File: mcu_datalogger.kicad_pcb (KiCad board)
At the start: 2 copper layers, 29 parts, among them J1 Conn_01x04_Pin, J2 Conn_01x04_Pin, J3 Conn_01x09_Pin, J4 Conn_02x03_Odd_Even, U1 24LC1025, U2 DS1337S_, U3 24LC1025, U4 ATMEGA328P-AU_SL044, Y1 32.768 KHz, Y2 16 MHz

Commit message: PCB v1
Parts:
- moved U3 38.7 mm to (161.1, 68.1), turned to -90 degrees
- moved R7 37.5 mm to (168.2, 87.0), turned to 180 degrees
- moved U1 37.5 mm to (167.1, 68.1), turned to -90 degrees
- moved R5 36.2 mm to (168.2, 89.0), turned to 180 degrees
- moved R3 34.6 mm to (165.3, 75.6), turned to 90 degrees
- moved R4 33.3 mm to (162.9, 75.6), turned to 90 degrees
- moved R6 30.4 mm to (155.4, 74.7), turned to -90 degrees
- moved Y2 28.5 mm to (146.9, 83.4), turned to 90 degrees
- moved J4 27.6 mm to (150.8, 67.8), turned to 90 degrees
- moved R1 27.1 mm to (154.6, 94.6), turned to 90 degrees
- moved C4 26.4 mm to (168.2, 85.0), turned to 180 degrees
- moved R2 25.9 mm to (152.5, 98.4), turned to 90 degrees
- moved J2 25.7 mm to (146.8, 65.3)
- moved C5 24.4 mm to (164.7, 87.0)
- moved Y1 23.1 mm to (156.7, 90.7)
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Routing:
- net GND: track 0.00 -> 194.3 mm, vias 0 -> 6
- net /Vcc: track 0.00 -> 139.6 mm, vias 0 -> 2
- net /SCK: track 0.00 -> 84.2 mm, vias 0 -> 2
- net /SDA: track 0.00 -> 66.4 mm, vias 0 -> 2
- net /D8: track 0.00 -> 30.9 mm, vias 0 -> 2
- net /D5: track 0.00 -> 30.6 mm, vias 0 -> 2
- net /D7: track 0.00 -> 30.4 mm, vias 0 -> 2
- net /D6: track 0.00 -> 30.1 mm, vias 0 -> 2
- net /MOSI: track 0.00 -> 26.0 mm, vias 0 -> 2
- net /MISO: track 0.00 -> 25.7 mm, vias 0 -> 2
- net /D4: track 0.00 -> 22.4 mm, vias 0 -> 2
- net /D2: track 0.00 -> 22.3 mm, vias 0 -> 2
- net /D3: track 0.00 -> 22.0 mm, vias 0 -> 2
- net Net-(BT1-+): track 0.00 -> 19.3 mm
- net /RX: track 0.00 -> 13.0 mm
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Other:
- board outline added: 30.3 x 39.1 mm

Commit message: PCB v2
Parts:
- moved H1 65.9 mm to (175.2, 60.8)
- moved H4 51.1 mm to (175.2, 102.0)
- moved H3 28.2 mm to (142.8, 102.0)
- moved H2 27.9 mm to (142.8, 60.8)
- moved BT1 17.0 mm to (164.6, 99.0)
- moved C1 0.68 mm to (154.3, 97.7)
- moved C2 0.68 mm to (146.6, 77.1)
- moved C4 0.68 mm to (167.9, 84.4)
- moved C5 0.68 mm to (164.4, 86.4)
- moved D1 0.68 mm to (164.4, 88.4)
- moved D2 0.68 mm to (164.4, 84.4)
- moved J1 0.68 mm to (171.9, 64.7)
- moved J3 0.68 mm to (171.9, 75.9)
- moved R1 0.68 mm to (154.3, 93.9)
- moved R2 0.68 mm to (152.2, 97.7)
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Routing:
- net Net-(BT1-+): track 19.3 -> 59.8 mm, vias 0 -> 2
- net Net-(U4-AREF): track 11.6 -> 8.68 mm, vias 0 -> 2
- net /D4: track 22.4 -> 21.1 mm

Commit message: PCB final
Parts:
- moved J3 25.4 mm to (146.5, 76.0)
- moved Y2 20.1 mm to (166.7, 82.9)
- moved C2 17.3 mm to (163.7, 80.0), turned to -90 degrees
- moved C3 17.3 mm to (163.7, 85.8), turned to 90 degrees
- moved C4 10.5 mm to (167.3, 94.9), turned to 0 degrees
- moved D2 7.14 mm to (167.3, 90.9)
- moved D1 6.56 mm to (163.8, 94.9)
- moved R7 6.55 mm to (167.3, 92.9), turned to 0 degrees
- moved R5 6.10 mm to (163.8, 92.9)
- moved C5 4.57 mm to (163.8, 90.9)
- moved J1 1.13 mm to (171.8, 65.8)
- moved R1 1.12 mm to (153.3, 93.5), turned to 0 degrees
- moved H1 0.28 mm to (175.0, 61.0)
- moved H2 0.28 mm to (143.0, 61.0)
- moved H3 0.20 mm to (143.0, 102.0)
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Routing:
- net GND: track 194.2 -> 166.9 mm, vias 6 -> 4
- net Net-(BT1-+): track 59.8 -> 34.9 mm
- net /D5: track 30.6 -> 7.45 mm, vias 2 -> 0
- net /D6: track 30.1 -> 8.60 mm, vias 2 -> 0
- net /D7: track 30.4 -> 9.17 mm, vias 2 -> 0
- net /D8: track 30.9 -> 10.9 mm, vias 2 -> 0
- net /D3: track 22.0 -> 5.11 mm, vias 2 -> 0
- net /D4: track 21.1 -> 5.01 mm, vias 2 -> 0
- net /D2: track 22.3 -> 7.04 mm, vias 2 -> 0
- net Net-(U4-AREF): track 8.68 -> 17.8 mm, vias 2 -> 0
- net Net-(U4-PB6): track 10.1 -> 18.7 mm, vias 0 -> 2
- net Net-(U4-PB7): track 8.22 -> 16.7 mm, vias 0 -> 2
- net /Vcc: track 139.6 -> 133.8 mm, vias 2 -> 0
- net Net-(U2-~{INTA}): track 4.79 -> 7.02 mm, vias 0 -> 2
- net /SDA: track 66.4 -> 68.3 mm
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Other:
- board size 30.3 x 39.1 mm -> 38 x 47 mm

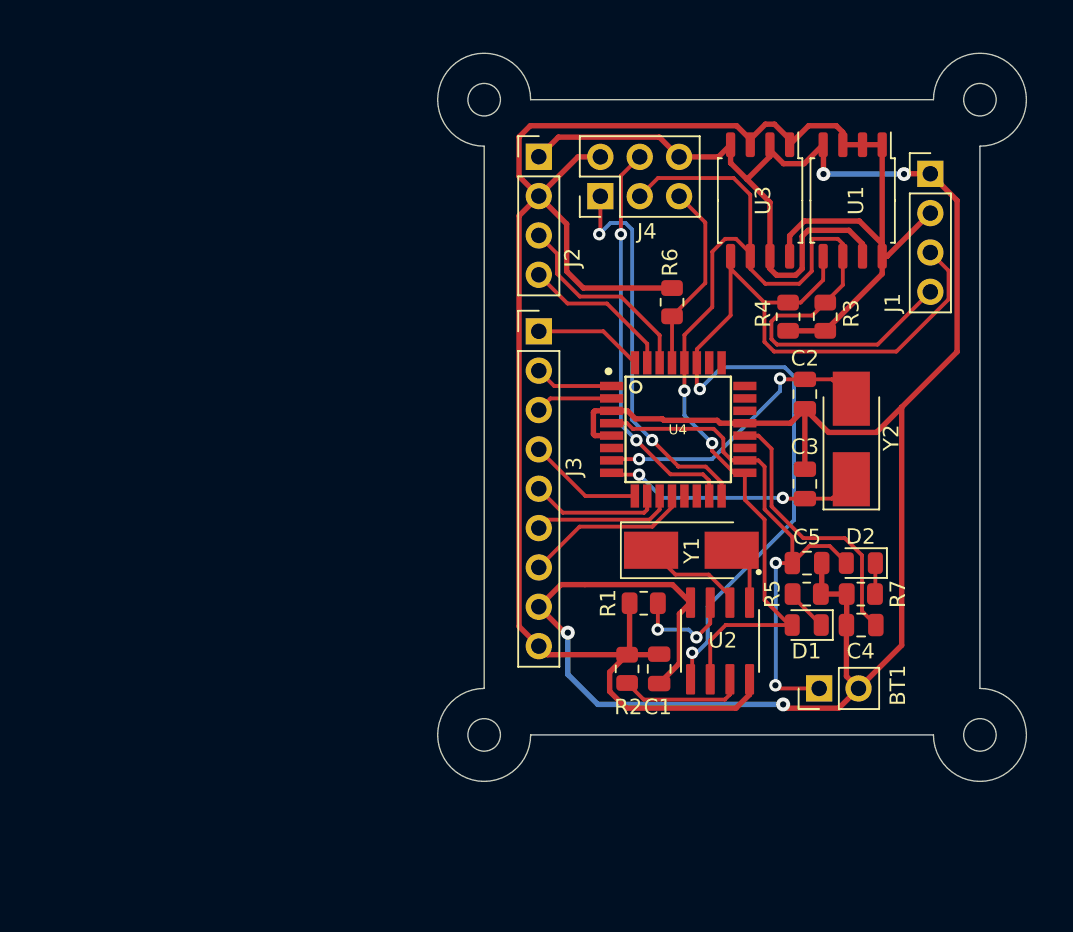
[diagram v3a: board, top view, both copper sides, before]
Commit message: PCB final v2
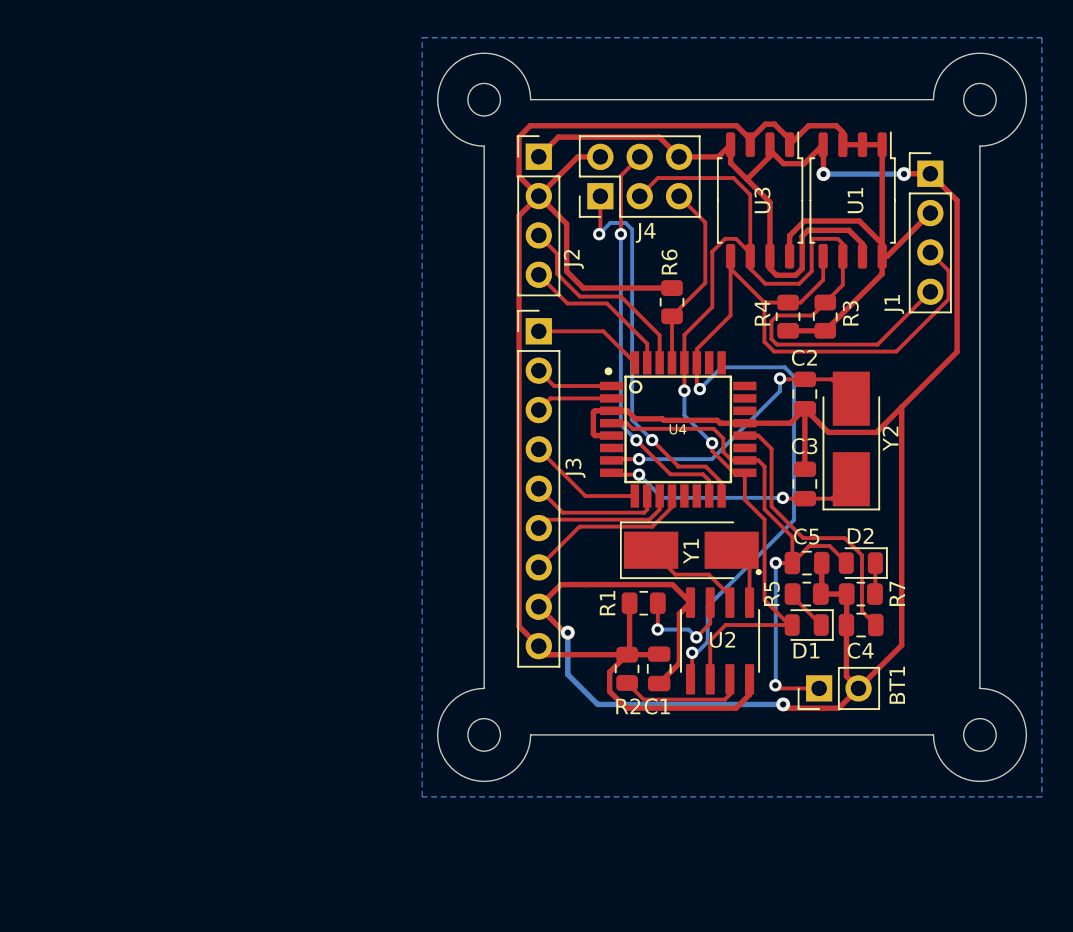
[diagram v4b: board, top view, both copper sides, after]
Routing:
- added copper zone on B.Cu, net GND
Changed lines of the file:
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@@
 		(net "Net-(U2-X2)")
+	)
+	(zone
+		(net "GND")
+		(layer "B.Cu")
+		(hatch edge 0.5)
+		(connect_pads
+			(clearance 0.5)
+		)
+		(min_thickness 0.25)
+		(fill yes
+			(thermal_gap 0.5)
+			(thermal_bridge_width 0.5)
+			(island_removal_mode 0)
+		)
+		(polygon
+			(pts
+				(xy 139 57) (xy 179 57) (xy 179 106) (xy 139 106)
+			)
+		)
 	)
 	(embedded_fonts no)

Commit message: PCB final v3
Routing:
- net /Vcc: track 133.8 -> 0.00 mm
- net GND: track 166.9 -> 110.8 mm, vias 4 -> 2
- added copper zone on F.Cu, net /Vcc

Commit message: Finished
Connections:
- BT1 pad 1: Net-(BT1-+) -> /Vcc
- C5 pad 1: Net-(BT1-+) -> /Vcc
- D2 pad 2: Net-(BT1-+) -> /Vcc
- U4 pad 18: Net-(BT1-+) -> /Vcc
- U4 pad 4: Net-(BT1-+) -> /Vcc
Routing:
- net Net-(BT1-+): track 34.8 -> 0.00 mm, vias 2 -> 0
- net /Vcc: track 0.00 -> 34.4 mm, vias 0 -> 2
- net Net-(U4-PB7): track 16.7 -> 34.0 mm
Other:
- board text added: "- 2MB EEPROM - RTC - I2C, SPI, GPIOs"
- board text added: "D2"
- board text added: "D3"
- board text added: "D4"
- board text added: "D5"
- board text added: "D6"
- board text added: "D7"
- board text added: "D8"
- board text added: "GND"
- board text added: "GPIO"
- board text added: "I2C"
- board text added: "ICSP"
- board text added: "MCU Datalogger"
- board text added: "MISO"
- board text added: "MOSI"
- board text added: "RESET"
- board text added: "RX"
- board text added: "SCK"
- board text added: "SDA"
- board text added: "SERIAL"
- board text added: "TX"
- board text added: "Vcc"

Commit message: bugfix
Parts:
- moved R3 12.4 mm to (152.9, 72.6)
- moved R6 1.50 mm to (155.4, 72.6), turned to 90 degrees
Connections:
- J1 pad 4: /SCK -> /SCL
- U1 pad 6: /SCK -> /SCL
- U2 pad 6: /SCK -> /SCL
- U3 pad 6: /SCK -> /SCL
- U4 pad 28: /SCK -> /SCL
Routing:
- net /SCL: track 0.00 -> 58.7 mm, vias 0 -> 2
- net /SCK: track 83.0 -> 37.0 mm
- net /SDA: track 68.3 -> 63.1 mm
- net Net-(U4-PB7): track 34.0 -> 35.2 mm
- net /RX: track 13.0 -> 12.0 mm
- net /RESET: track 12.3 -> 13.1 mm
